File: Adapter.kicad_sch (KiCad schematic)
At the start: 0 parts

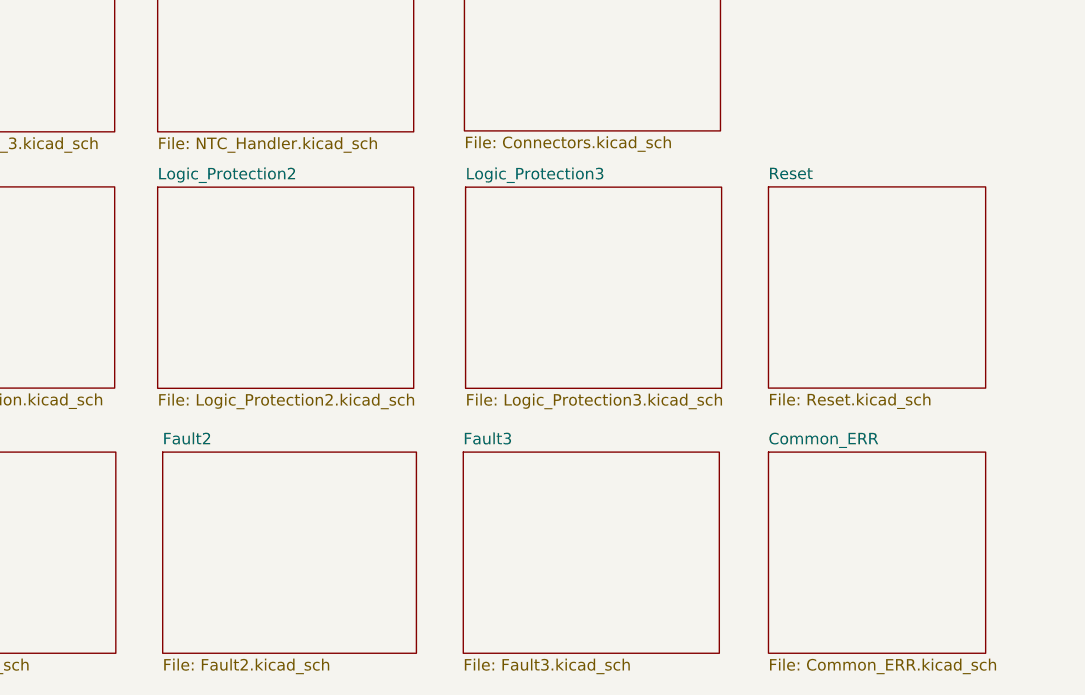
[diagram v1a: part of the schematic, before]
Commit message: Изменил схему
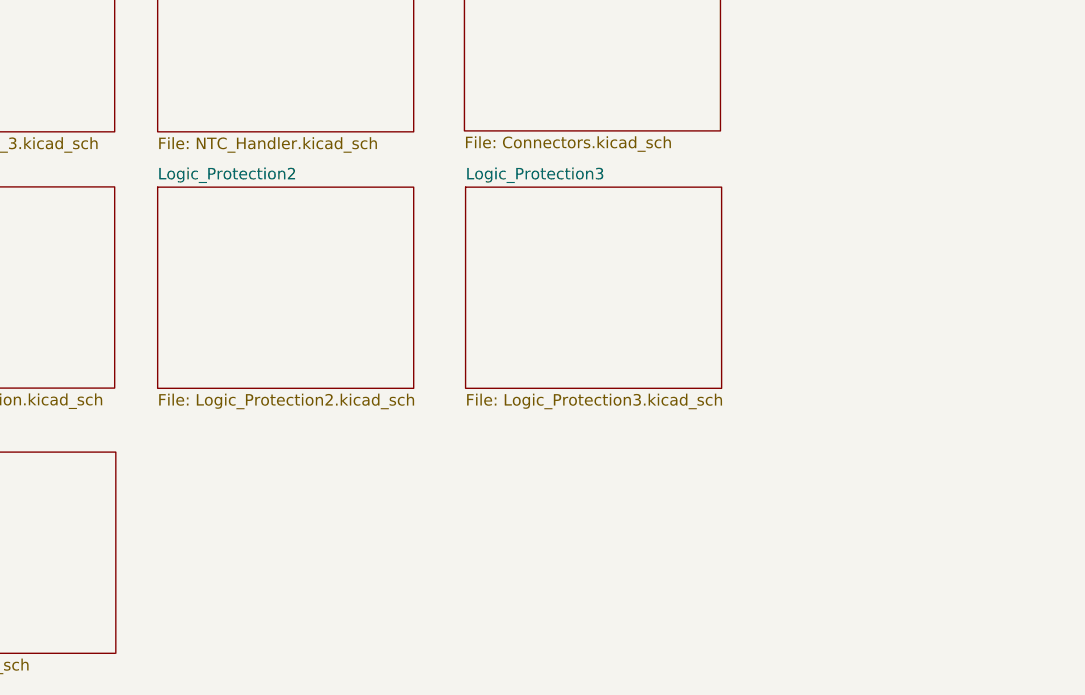
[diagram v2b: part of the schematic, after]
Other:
- removed sheet Common_ERR
- removed sheet Fault2
- removed sheet Fault3
- removed sheet Reset

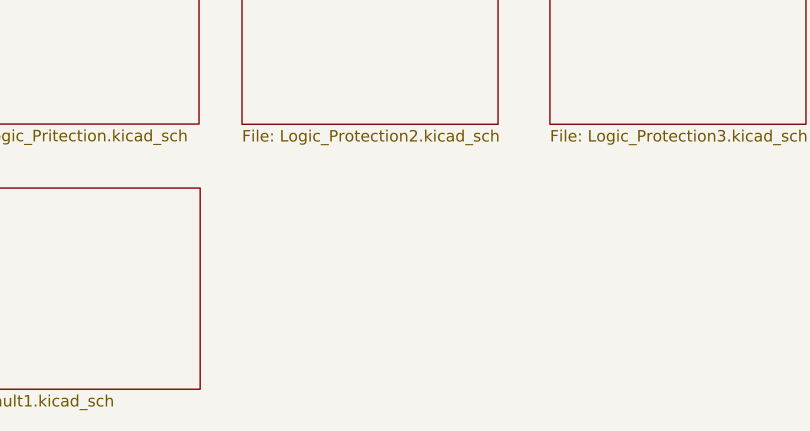
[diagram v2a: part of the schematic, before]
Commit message: Разместил все три стойки в своей области
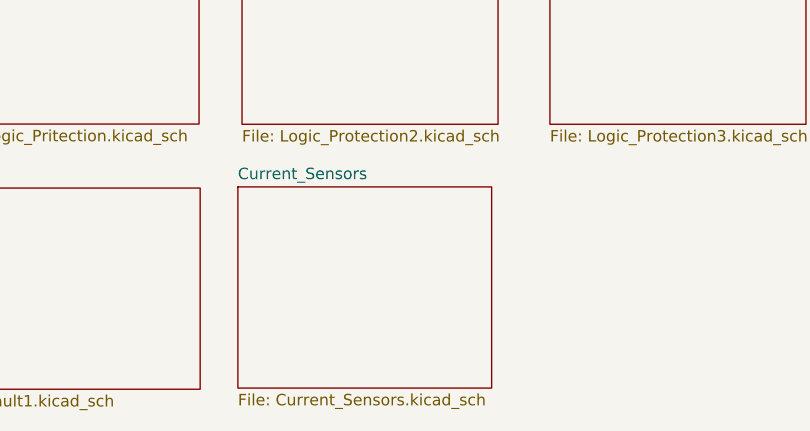
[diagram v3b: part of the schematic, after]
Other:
- added sheet Current_Sensors (Current_Sensors.kicad_sch)
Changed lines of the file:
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@@
+	)
+	(sheet
+		(at 50.8 167.64)
+		(size 28.194 22.352)
+		(fields_autoplaced yes)
+		(stroke
+			(width 0.1524)
+			(type solid)
+		)
+		(fill
+			(color 0 0 0 0.0000)
+		)
+		(property "Sheetname" "Current_Sensors"
+			(at 50.8 166.9284 0)
+			(effects
+				(font
+					(size 1.27 1.27)
+				)
+				(justify left bottom)
+			)
+		)
+		(property "Sheetfile" "Current_Sensors.kicad_sch"
+			(at 50.8 190.5766 0)
+			(effects
+				(font
+					(size 1.27 1.27)
+				)
+				(justify left top)
+			)
+		)
+		(instances
+			(project "Adapter"
+				(path "/e63e39d7-6ac0-4ffd-8aa3-1841a4541b55"
+					(page "4")
+				)
+			)
+		)
 	)
 	(sheet

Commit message: Добавил температурные контуры звщиты
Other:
- added sheet NTC_Reset_A (NTC_Reset_A.kicad_sch)
- added sheet NTC_Reset_B (NTC_Reset_B.kicad_sch)
- added sheet NTC_Reset_C (NTC_Reset_C.kicad_sch)
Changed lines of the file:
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@@
+	)
+	(sheet
+		(at 117.475 109.22)
+		(size 28.448 22.5552)
+		(fields_autoplaced yes)
+		(stroke
+			(width 0.1524)
+			(type solid)
+		)
+		(fill
+			(color 0 0 0 0.0000)
+		)
+		(property "Sheetname" "NTC_Reset_A"
+			(at 117.475 108.5084 0)
+			(effects
+				(font
+					(size 1.27 1.27)
+				)
+				(justify left bottom)
+			)
+		)
+		(property "Sheetfile" "NTC_Reset_A.kicad_sch"
+			(at 117.475 132.3598 0)
+			(effects
+				(font
+					(size 1.27 1.27)
+				)
+				(justify left top)
+			)
+		)
+		(instances
+			(project "Adapter"
+				(path "/e63e39d7-6ac0-4ffd-8aa3-1841a4541b55"
+					(page "5")
+				)
+			)
+		)
 	)
 	(sheet
@@
 				)
 			)
+		)
+	)
+	(sheet
+		(at 177.165 109.22)
+		(size 28.448 22.5552)
+		(fields_autoplaced yes)
+		(stroke
+			(width 0.1524)
+			(type solid)
+		)
+		(fill
+			(color 0 0 0 0.0000)
+		)
+		(property "Sheetname" "NTC_Reset_C"
+			(at 177.165 108.5084 0)
+			(effects
+				(font
+					(size 1.27 1.27)
+				)
+				(justify left bottom)
+			)
+		)
+		(property "Sheetfile" "NTC_Reset_C.kicad_sch"
+			(at 177.165 132.3598 0)
+			(effects
+				(font
+					(size 1.27 1.27)
+				)
+				(justify left top)
+			)
+		)
+		(instances
+			(project "Adapter"
+				(path "/e63e39d7-6ac0-4ffd-8aa3-1841a4541b55"
+					(page "18")
+				)
+			)
+		)
+	)
+	(sheet
+		(at 147.32 109.22)
+		(size 28.448 22.5552)
+		(fields_autoplaced yes)
+		(stroke
+			(width 0.1524)
+			(type solid)
+		)
+		(fill
+			(color 0 0 0 0.0000)
+		)
+		(property "Sheetname" "NTC_Reset_B"
+			(at 147.32 108.5084 0)
+			(effects
+				(font
+					(size 1.27 1.27)
+				)
+				(justify left bottom)
+			)
+		)
+		(property "Sheetfile" "NTC_Reset_B.kicad_sch"
+			(at 147.32 132.3598 0)
+			(effects
+				(font
+					(size 1.27 1.27)
+				)
+				(justify left top)
+			)
+		)
+		(instances
+			(project "Adapter"
+				(path "/e63e39d7-6ac0-4ffd-8aa3-1841a4541b55"
+					(page "8")
+				)
+			)

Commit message: Убрал питание 3.3В
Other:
- removed sheet NTC_Reset_A
- removed sheet NTC_Reset_B
- removed sheet NTC_Reset_C
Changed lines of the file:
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@@
-	)
-	(sheet
-		(at 117.475 109.22)
-		(size 28.448 22.5552)
-		(fields_autoplaced yes)
-		(stroke
-			(width 0.1524)
-			(type solid)
-		)
-		(fill
-			(color 0 0 0 0.0000)
-		)
-		(property "Sheetname" "NTC_Reset_A"
-			(at 117.475 108.5084 0)
-			(effects
-				(font
-					(size 1.27 1.27)
-				)
-				(justify left bottom)
-			)
-		)
-		(property "Sheetfile" "NTC_Reset_A.kicad_sch"
-			(at 117.475 132.3598 0)
-			(effects
-				(font
-					(size 1.27 1.27)
-				)
-				(justify left top)
-			)
-		)
-		(instances
-			(project "Adapter"
-				(path "/e63e39d7-6ac0-4ffd-8aa3-1841a4541b55"
-					(page "5")
-				)
-			)
-		)
 	)
 	(sheet
@@
 				)
 			)
-		)
-	)
-	(sheet
-		(at 177.165 109.22)
-		(size 28.448 22.5552)
-		(fields_autoplaced yes)
-		(stroke
-			(width 0.1524)
-			(type solid)
-		)
-		(fill
-			(color 0 0 0 0.0000)
-		)
-		(property "Sheetname" "NTC_Reset_C"
-			(at 177.165 108.5084 0)
-			(effects
-				(font
-					(size 1.27 1.27)
-				)
-				(justify left bottom)
-			)
-		)
-		(property "Sheetfile" "NTC_Reset_C.kicad_sch"
-			(at 177.165 132.3598 0)
-			(effects
-				(font
-					(size 1.27 1.27)
-				)
-				(justify left top)
-			)
-		)
-		(instances
-			(project "Adapter"
-				(path "/e63e39d7-6ac0-4ffd-8aa3-1841a4541b55"
-					(page "18")
-				)
-			)
-		)
-	)
-	(sheet
-		(at 147.32 109.22)
-		(size 28.448 22.5552)
-		(fields_autoplaced yes)
-		(stroke
-			(width 0.1524)
-			(type solid)
-		)
-		(fill
-			(color 0 0 0 0.0000)
-		)
-		(property "Sheetname" "NTC_Reset_B"
-			(at 147.32 108.5084 0)
-			(effects
-				(font
-					(size 1.27 1.27)
-				)
-				(justify left bottom)
-			)
-		)
-		(property "Sheetfile" "NTC_Reset_B.kicad_sch"
-			(at 147.32 132.3598 0)
-			(effects
-				(font
-					(size 1.27 1.27)
-				)
-				(justify left top)
-			)
-		)
-		(instances
-			(project "Adapter"
-				(path "/e63e39d7-6ac0-4ffd-8aa3-1841a4541b55"
-					(page "8")
-				)
-			)

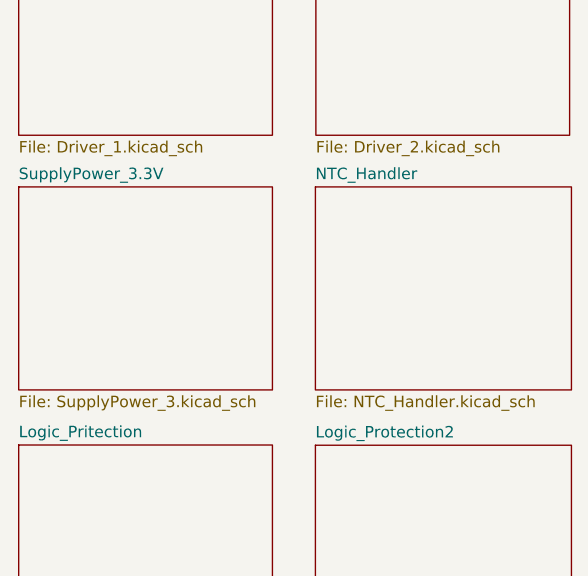
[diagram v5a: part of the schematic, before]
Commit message: Развел стойку фазы А
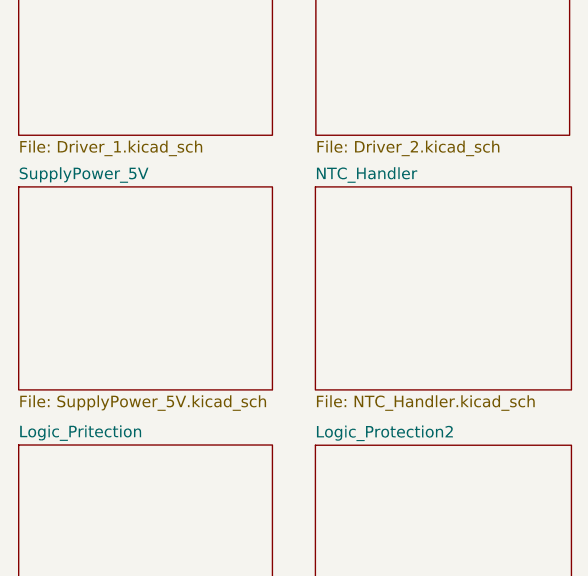
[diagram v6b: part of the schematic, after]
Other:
- sheet SupplyPower_3.3V renamed SupplyPower_5V
- sheet SupplyPower_5V: file SupplyPower_3.kicad_sch -> SupplyPower_5V.kicad_sch
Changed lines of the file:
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@@
 			(color 0 0 0 0.0000)
 		)
-		(property "Sheetname" "SupplyPower_3.3V"
+		(property "Sheetname" "SupplyPower_5V"
 			(at 18.288 108.9148 0)
 			(effects
@@
 			)
 		)
-		(property "Sheetfile" "SupplyPower_3.kicad_sch"
+		(property "Sheetfile" "SupplyPower_5V.kicad_sch"
 			(at 18.288 132.7662 0)
 			(effects
